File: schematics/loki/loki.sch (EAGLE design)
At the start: 54 parts, among them IC2 LM358D, Q1 MOSFET-PCHANNELSMD, U1 USD SOCKET, Y1 XRCGB_XTAL

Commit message: Misc tweaks, generated gerbers.
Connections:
- net SCL0: now also SV1.5; no longer SV1.4
- net SDA0: now also SV1.4; no longer SV1.5
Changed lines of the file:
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@@
-</segment>
-<segment>
-<pinref part="SV1" gate="G$1" pin="4"/>
-<wire x1="381" y1="0" x2="386.08" y2="0" width="0.1524" layer="91"/>
-<label x="381" y="0" size="1.778" layer="95"/>
 </segment>
 <segment>
@@
 <label x="490.22" y="142.24" size="1.778" layer="95"/>
 </segment>
+<segment>
+<pinref part="SV1" gate="G$1" pin="5"/>
+<wire x1="381" y1="-2.54" x2="386.08" y2="-2.54" width="0.1524" layer="91"/>
+<label x="381" y="-2.54" size="1.778" layer="95"/>
+</segment>
 </net>
 <net name="SDA0" class="0">
@@
 <wire x1="375.92" y1="170.18" x2="381" y2="170.18" width="0.1524" layer="91"/>
 <label x="378.46" y="170.18" size="1.778" layer="95"/>
-</segment>
-<segment>
-<pinref part="SV1" gate="G$1" pin="5"/>
-<wire x1="381" y1="-2.54" x2="386.08" y2="-2.54" width="0.1524" layer="91"/>
-<label x="381" y="-2.54" size="1.778" layer="95"/>
 </segment>
 <segment>
@@
 <label x="497.84" y="139.7" size="1.778" layer="95"/>
 </segment>
+<segment>
+<pinref part="SV1" gate="G$1" pin="4"/>
+<wire x1="381" y1="0" x2="386.08" y2="0" width="0.1524" layer="91"/>
+<label x="381" y="0" size="1.778" layer="95"/>
+</segment>
 </net>

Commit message: Reworked Loki to fit the 100TQFP package.
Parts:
- removed U$1: CY83XXX-68PIN, cypress_psoc_V1_0:CY83XXX-68PIN
- added U2: CY8C5XXX-100PIN, cypress_psoc_V1_0:CY8C5XXX-100PIN
- C3: value 0.1u -> 1u; device resistor:C-EUC0603K -> resistor:C-USC0603
- U$9: device SparkFun-Passives:GND_CONNECT -> nickparts:GND_CONNECT
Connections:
- net N$11 renamed DCIN
- net N$15 renamed VBUS
- net N$2 renamed D-IN
- net N$4 renamed D+IN
- net N$6 renamed BOOST
- net N$7 renamed INDIN
- net N$8 renamed FB
- removed net N$16: C4.1, U$1.P15[0], Y1.2
- removed net N$17: C5.1, U$1.P15[1], Y1.1
- removed net N$20: C7.1, R9.1, S1.2, U$1.P12[2]
- removed net P0[0]: U$1.P0[0], U$5.12
- removed net P0[1]: U$1.P0[1], U$5.11
- removed net P0[2]: U$1.P0[2], U$5.14
- removed net P0[3]: U$1.P0[3], U$5.13
- removed net P0[4]: U$1.P0[4], U$5.16
- removed net P0[5]: U$1.P0[5], U$5.15
- removed net P0[6]: U$1.P0[6], U$5.18
- removed net P0[7]: U$1.P0[7], U$5.17
- removed net P15[2]: U$1.P15[2], U$5.10
- removed net P15[3]: U$1.P15[3], U$5.9
- removed net P15[5]: U$1.P15[5], U$5.20
- removed net P1[2]: U$1.P1[2], U$5.27
- removed net P1[4]: U$1.P1[4], U$5.30
- removed net P1[6]: U$1.P1[6], U$5.32
- removed net P1[7]: U$1.P1[7], U$5.31
- removed net P2[0]: U$1.P2[0], U$5.19
- removed net P2[1]: U$1.P2[1], U$5.22
- removed net P2[2]: U$1.P2[2], U$5.21
- removed net P2[3]: U$1.P2[3], U$5.24
- removed net P2[4]: U$1.P2[4], U$5.23
- removed net P2[5]: U$1.P2[5], U$5.26
- removed net P2[6]: U$1.P2[6], U$5.25
- removed net P2[7]: U$1.P2[7], U$5.28
- removed net P3[0]: U$1.P3[0], U$5.2
- removed net P3[1]: U$1.P3[1], U$5.1
- removed net P3[2]: U$1.P3[2], U$5.4
- removed net P3[3]: U$1.P3[3], U$5.3
- removed net P3[4]: U$1.P3[4], U$5.6
- removed net P3[5]: U$1.P3[5], U$5.5
- removed net P3[6]: U$1.P3[6], U$5.8
- removed net P3[7]: U$1.P3[7], U$5.7
- new net CLKI: C4.1, U2.P15_1_MXTLI, Y1.2
- new net CLKO: C5.1, U2.P15_0_MXTLO, Y1.1
- new net GPIO1: U$5.2, U2.P3_0
- new net GPIO10: U$5.9, U2.P15_3_KXTLI
- new net GPIO11: U$5.12, U2.P4_0
- new net GPIO12: U$5.11, U2.P4_1
- new net GPIO13: U$5.14, U2.P4_2
- new net GPIO14: U$5.13, U2.P4_3
- new net GPIO15: U$5.16, U2.P4_4
- new net GPIO16: U$5.15, U2.P4_5
- new net GPIO17: U$5.18, U2.P0_0
- new net GPIO18: U$5.17, U2.P0_1
- new net GPIO19: U$5.20, U2.P0_2
- new net GPIO2: U$5.1, U2.P3_1
- new net GPIO20: U$5.19, U2.P0_3
- new net GPIO21: U$5.22, U2.P0_4
- new net GPIO22: U$5.21, U2.P0_5
- new net GPIO23: U$5.24, U2.P0_6
- new net GPIO24: U$5.23, U2.P0_7
- new net GPIO25: U$5.26, U2.P4_6
- new net GPIO26: U$5.25, U2.P4_7
- new net GPIO27: U$5.28, U2.P6_0
- new net GPIO28: U$5.27, U2.P6_1
- new net GPIO29: U$5.30, U2.P6_2
- new net GPIO3: U$5.4, U2.P3_2
- new net GPIO30: U$5.29, U2.P6_3
- new net GPIO31: U$5.32, U2.P15_4
- new net GPIO32: U$5.31, U2.P15_5
- new net GPIO4: U$5.3, U2.P3_3
- new net GPIO5: U$5.6, U2.P3_4
- new net GPIO6: U$5.5, U2.P3_5
- new net GPIO7: U$5.8, U2.P3_6
- new net GPIO8: U$5.7, U2.P3_7
- new net GPIO9: U$5.10, U2.P15_2_KXTLO
- new net N$2: R3.2, U2.P2_5
- new net TDI: U$2.8, U2.P1_4_TDI
- new net VCCD: C15.1, U2.VCCD@39, U2.VCCD@86
- net +3V3: now also U2.VDDA@65, U2.VDDD@37, U2.VDDD@88, U2.VDDIO0@75, U2.VDDIO1@26, U2.VDDIO2@100, U2.VDDIO3@50; no longer C17.1, U$1.VDDA, U$1.VDDD, U$1.VDDIO0, U$1.VDDIO1, U$1.VDDIO2, U$1.VDDIO3, U$2.1
- net +5V: now also C17.1, C3.1, U$2.1
- net AGND: now also U2.VSSA@64; no longer U$1.VSSA
- net D+: now also U2.P15_6_DP; no longer U$1.P15[6]
- net D-: now also U2.P15_7_DM; no longer U$1.P15[7]
- net DGND: now also U2.VSSD@10, U2.VSSD@12, U2.VSSD@13, U2.VSSD@14, U2.VSSD@38, U2.VSSD@66, U2.VSSD@87; no longer C3.2, U$1.VBAT, U$1.VBOOST, U$1.VSSB, U$1.VSSD
- net GND: now also C3.2
- net N$1: now also U2.P12_2; no longer C15.1, C3.1, U$1.VCCD
- net N$10: now also U2.P12_3; no longer R3.2, U$1.P12[3]
- net N$3: now also U2.VCCA@63; no longer U$1.VCCA
- net P1[5]: now also C7.1, R9.1, S1.2, U2.P1_5_NTRST; no longer U$1.P1[5], U$5.29
- net SCL0: now also U2.P12_4_I2C0_SCL; no longer U$1.P12[4]
- net SDA0: now also U2.P12_5_I2C0_SDA; no longer U$1.P12[5]
- net SWDCK: now also U2.P1_1_TCK_SWDCK; no longer U$1.P1[1]
- net SWDIO: now also U2.P1_0_TMS_SWDIO; no longer U$1.P1[0]
- net SWV: now also U2.P1_3_TDO_SWV; no longer U$1.P1[3]
- net USD_CD: now also U2.P6_7; no longer U$1.P15[4]
- net USD_CS: now also U2.P5_3; no longer U$1.P12[6]
- net USD_DI: now also U2.P5_2; no longer U$1.P12[7]
- net USD_DO: now also U2.P5_0; no longer U$1.P12[0]
- net USD_SCK: now also U2.P5_1; no longer U$1.P12[1]
- net XRES: now also U2.!XRES!; no longer U$1.XRES
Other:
- moved on the sheet: C1, C10, C11, C12, C13, C14, C15, C2, C3, C4, C5, C6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

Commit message: Misc layout improvements to Loki; updated to v0.2.
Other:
- moved on the sheet: C1, C10, C11, C12, C13, C14, C15, C16, C17, C18, C19, C2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

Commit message: Added missing gerbers and loki schematic
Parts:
- U2: value CY8C5XXX-100PIN -> CY8C5XXX
- renumbered U$11 to U6, U$2 to U3, U$3 to U4, U$4 to U5, U$7 to U7

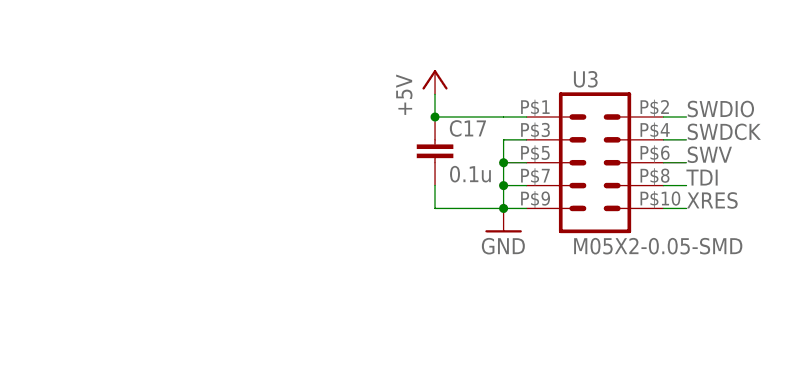
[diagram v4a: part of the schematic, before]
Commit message: Fixed both Loki and the programmer to use 3.3v for power on programming headers.
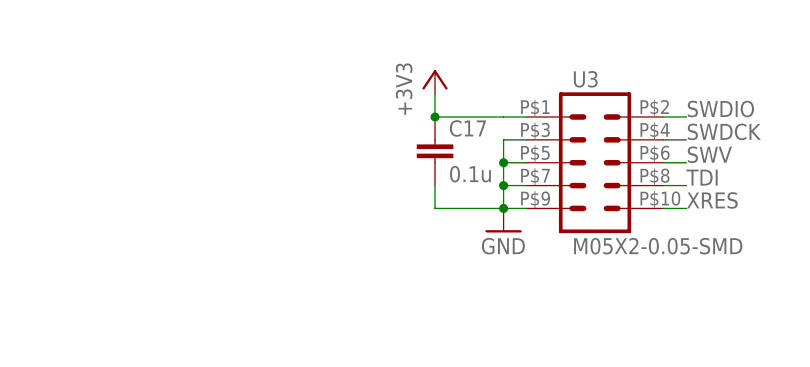
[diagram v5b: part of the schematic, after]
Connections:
- net +3V3: now also C17.1, U3.1
- net +5V: no longer C17.1, U3.1
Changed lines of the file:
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@@
 <part name="SUPPLY10" library="supply2" deviceset="DGND" device=""/>
 <part name="VCC7" library="supply1" deviceset="+3V3" device=""/>
-<part name="P+4" library="supply1" deviceset="+5V" device=""/>
 <part name="C3" library="resistor" deviceset="C-US" device="C0603" value="1u"/>
+<part name="+3V5" library="supply1" deviceset="+3V3" device=""/>
 </parts>
 <sheets>
@@
 <instance part="SUPPLY10" gate="G$1" x="190.5" y="172.72"/>
 <instance part="VCC7" gate="G$1" x="111.76" y="243.84"/>
-<instance part="P+4" gate="1" x="228.6" y="243.84"/>
 <instance part="C3" gate="G$1" x="335.28" y="172.72"/>
+<instance part="+3V5" gate="G$1" x="228.6" y="243.84"/>
 </instances>
 <busses>
@@
 <wire x1="121.92" y1="33.02" x2="101.6" y2="33.02" width="0.1524" layer="91"/>
 </segment>
-<segment>
-<pinref part="U3" gate="G$1" pin="1"/>
-<wire x1="238.76" y1="238.76" x2="236.22" y2="238.76" width="0.1524" layer="91"/>
-<pinref part="C17" gate="G$1" pin="1"/>
-<wire x1="236.22" y1="238.76" x2="228.6" y2="238.76" width="0.1524" layer="91"/>
-<wire x1="228.6" y1="238.76" x2="228.6" y2="241.3" width="0.1524" layer="91"/>
-<junction x="228.6" y="238.76"/>
-<pinref part="P+4" gate="1" pin="+5V"/>
-</segment>
 </net>
 <net name="+3V3" class="0">
@@
 <junction x="111.76" y="241.3"/>
 </segment>
+<segment>
+<pinref part="U3" gate="G$1" pin="1"/>
+<wire x1="238.76" y1="238.76" x2="236.22" y2="238.76" width="0.1524" layer="91"/>
+<pinref part="C17" gate="G$1" pin="1"/>
+<wire x1="236.22" y1="238.76" x2="228.6" y2="238.76" width="0.1524" layer="91"/>
+<wire x1="228.6" y1="238.76" x2="228.6" y2="241.3" width="0.1524" layer="91"/>
+<junction x="228.6" y="238.76"/>
+<pinref part="+3V5" gate="G$1" pin="+3V3"/>
+</segment>
 </net>
